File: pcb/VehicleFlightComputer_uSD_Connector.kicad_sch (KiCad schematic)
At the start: 10 parts, among them J5 0472192001

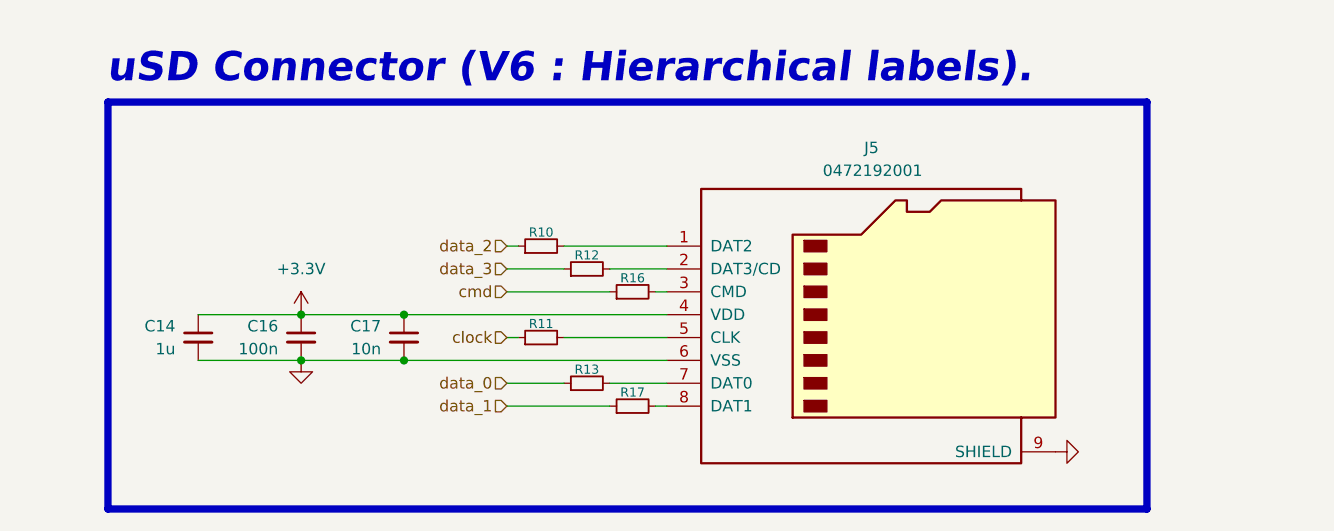
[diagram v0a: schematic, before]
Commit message: Added uSD connector for `VehicleFlightComputer`; added missing solder jumper footprint for LSM6DSV32X.
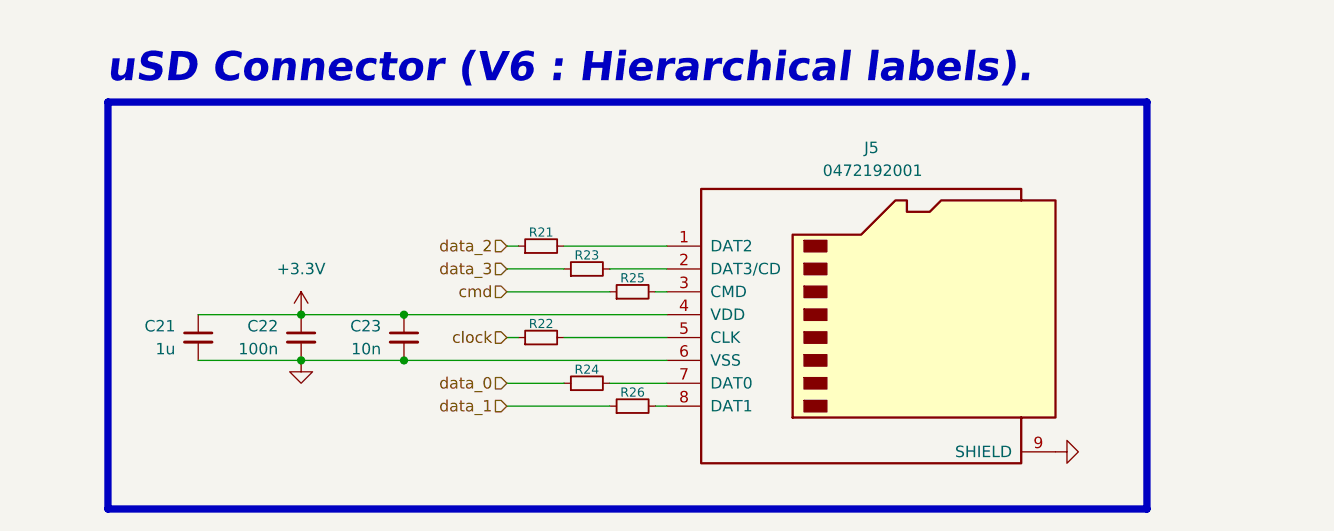
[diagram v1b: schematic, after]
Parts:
- renumbered C14 to C21, C16 to C22, C17 to C23, R10 to R21, R11 to R22, R12 to R23, R13 to R24, R16 to R25, R17 to R26
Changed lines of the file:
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@@
 		(on_board yes)
 		(dnp no)
-		(property "Reference" "R10"
+		(property "Reference" "R21"
 			(at 92.71 68.326 90)
 			(effects
@@
 		(instances
 			(project "VehicleFlightComputer"
-				(path "/378ff2fd-4011-4cd9-8b06-ddd39885e073/6e13037a-c249-4898-9fed-e095c84fcb99"
-					(reference "R10")
+				(path "/378ff2fd-4011-4cd9-8b06-ddd39885e073/759d802d-72f0-4543-9abd-1bdb6f3a2344"
+					(reference "R21")
 					(unit 1)
 				)
@@
 		(on_board yes)
 		(dnp no)
-		(property "Reference" "R11"
+		(property "Reference" "R22"
 			(at 92.71 78.486 90)
 			(effects
@@
 		(instances
 			(project "VehicleFlightComputer"
-				(path "/378ff2fd-4011-4cd9-8b06-ddd39885e073/6e13037a-c249-4898-9fed-e095c84fcb99"
-					(reference "R11")
+				(path "/378ff2fd-4011-4cd9-8b06-ddd39885e073/759d802d-72f0-4543-9abd-1bdb6f3a2344"
+					(reference "R22")
 					(unit 1)
 				)
@@
 		(on_board yes)
 		(dnp no)
-		(property "Reference" "R12"
+		(property "Reference" "R23"
 			(at 97.79 70.866 90)
 			(effects
@@
 		(instances
 			(project "VehicleFlightComputer"
-				(path "/378ff2fd-4011-4cd9-8b06-ddd39885e073/6e13037a-c249-4898-9fed-e095c84fcb99"
-					(reference "R12")
+				(path "/378ff2fd-4011-4cd9-8b06-ddd39885e073/759d802d-72f0-4543-9abd-1bdb6f3a2344"
+					(reference "R23")
 					(unit 1)
 				)
@@
 		(on_board yes)
 		(dnp no)
-		(property "Reference" "R13"
+		(property "Reference" "R24"
 			(at 97.79 83.566 90)
 			(effects
@@
 		(instances
 			(project "VehicleFlightComputer"
-				(path "/378ff2fd-4011-4cd9-8b06-ddd39885e073/6e13037a-c249-4898-9fed-e095c84fcb99"
-					(reference "R13")
+				(path "/378ff2fd-4011-4cd9-8b06-ddd39885e073/759d802d-72f0-4543-9abd-1bdb6f3a2344"
+					(reference "R24")
 					(unit 1)
 				)
@@
 		(on_board yes)
 		(dnp no)
-		(property "Reference" "R16"
+		(property "Reference" "R25"
 			(at 102.87 73.406 90)
 			(effects
@@
 		(instances
 			(project "VehicleFlightComputer"
-				(path "/378ff2fd-4011-4cd9-8b06-ddd39885e073/6e13037a-c249-4898-9fed-e095c84fcb99"
-					(reference "R16")
+				(path "/378ff2fd-4011-4cd9-8b06-ddd39885e073/759d802d-72f0-4543-9abd-1bdb6f3a2344"
+					(reference "R25")
 					(unit 1)
 				)
@@
 		(on_board yes)
 		(dnp no)
-		(property "Reference" "C14"
+		(property "Reference" "C21"
 			(at 52.07 78.7462 0)
 			(effects
@@
 		(instances
 			(project "VehicleFlightComputer"
-				(path "/378ff2fd-4011-4cd9-8b06-ddd39885e073/6e13037a-c249-4898-9fed-e095c84fcb99"
-					(reference "C14")
+				(path "/378ff2fd-4011-4cd9-8b06-ddd39885e073/759d802d-72f0-4543-9abd-1bdb6f3a2344"
+					(reference "C21")
 					(unit 1)
 				)
@@
 		(on_board yes)
 		(dnp no)
-		(property "Reference" "C16"
+		(property "Reference" "C22"
 			(at 63.5 78.7462 0)
 			(effects
@@
 		(instances
 			(project "VehicleFlightComputer"
-				(path "/378ff2fd-4011-4cd9-8b06-ddd39885e073/6e13037a-c249-4898-9fed-e095c84fcb99"
-					(reference "C16")
+				(path "/378ff2fd-4011-4cd9-8b06-ddd39885e073/759d802d-72f0-4543-9abd-1bdb6f3a2344"
+					(reference "C22")
 					(unit 1)
 				)
@@
 		(instances
 			(project "VehicleFlightComputer"
-				(path "/378ff2fd-4011-4cd9-8b06-ddd39885e073/6e13037a-c249-4898-9fed-e095c84fcb99"
+				(path "/378ff2fd-4011-4cd9-8b06-ddd39885e073/759d802d-72f0-4543-9abd-1bdb6f3a2344"
 					(reference "J5")
 					(unit 1)
@@
 		(dnp no)
 		(fields_autoplaced yes)
-		(property "Reference" "#PWR033"
+		(property "Reference" "#PWR076"
 			(at 66.04 88.9 0)
 			(effects
@@
 		(instances
 			(project "VehicleFlightComputer"
-				(path "/378ff2fd-4011-4cd9-8b06-ddd39885e073/6e13037a-c249-4898-9fed-e095c84fcb99"
-					(reference "#PWR033")
+				(path "/378ff2fd-4011-4cd9-8b06-ddd39885e073/759d802d-72f0-4543-9abd-1bdb6f3a2344"
+					(reference "#PWR076")
 					(unit 1)
 				)
@@
 		(dnp no)
 		(fields_autoplaced yes)
-		(property "Reference" "#PWR032"
+		(property "Reference" "#PWR075"
 			(at 66.04 81.28 0)
 			(effects
@@
 		(instances
 			(project "VehicleFlightComputer"
-				(path "/378ff2fd-4011-4cd9-8b06-ddd39885e073/6e13037a-c249-4898-9fed-e095c84fcb99"
-					(reference "#PWR032")
+				(path "/378ff2fd-4011-4cd9-8b06-ddd39885e073/759d802d-72f0-4543-9abd-1bdb6f3a2344"
+					(reference "#PWR075")
 					(unit 1)
 				)
@@
 		(dnp no)
 		(fields_autoplaced yes)
-		(property "Reference" "#PWR037"
+		(property "Reference" "#PWR077"
 			(at 156.21 92.71 0)
 			(effects
@@
 		(instances
 			(project "VehicleFlightComputer"
-				(path "/378ff2fd-4011-4cd9-8b06-ddd39885e073/6e13037a-c249-4898-9fed-e095c84fcb99"
-					(reference "#PWR037")
+				(path "/378ff2fd-4011-4cd9-8b06-ddd39885e073/759d802d-72f0-4543-9abd-1bdb6f3a2344"
+					(reference "#PWR077")
 					(unit 1)
 				)
@@
 		(on_board yes)
 		(dnp no)
-		(property "Reference" "R17"
+		(property "Reference" "R26"
 			(at 102.87 86.106 90)
 			(effects
@@
 		(instances
 			(project "VehicleFlightComputer"
-				(path "/378ff2fd-4011-4cd9-8b06-ddd39885e073/6e13037a-c249-4898-9fed-e095c84fcb99"
-					(reference "R17")
+				(path "/378ff2fd-4011-4cd9-8b06-ddd39885e073/759d802d-72f0-4543-9abd-1bdb6f3a2344"
+					(reference "R26")
 					(unit 1)
 				)
@@
 		(on_board yes)
 		(dnp no)
-		(property "Reference" "C17"
+		(property "Reference" "C23"
 			(at 74.93 78.7462 0)
 			(effects
@@
 		(instances
 			(project "VehicleFlightComputer"
-				(path "/378ff2fd-4011-4cd9-8b06-ddd39885e073/6e13037a-c249-4898-9fed-e095c84fcb99"
-					(reference "C17")
-					(unit 1)
-				)
+				(path "/378ff2fd-4011-4cd9-8b06-ddd39885e073/759d802d-72f0-4543-9abd-1bdb6f3a2344"
+					(reference "C23")
+					(unit 1)
+				)

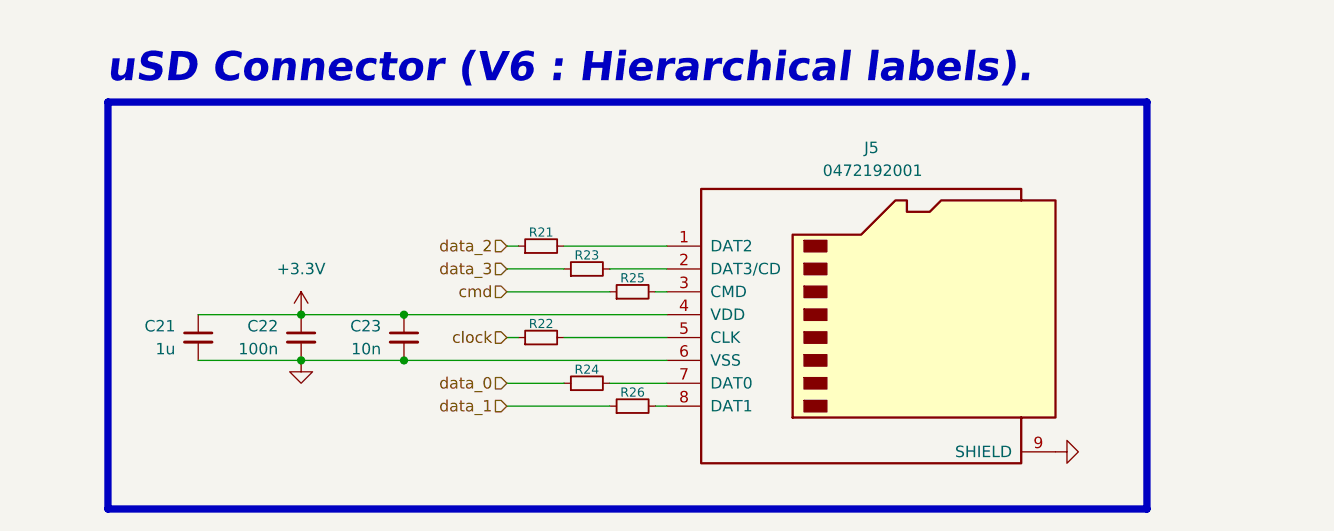
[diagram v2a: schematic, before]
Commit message: Addressed ERC schematic issues for `VehicleFlightComputer`.
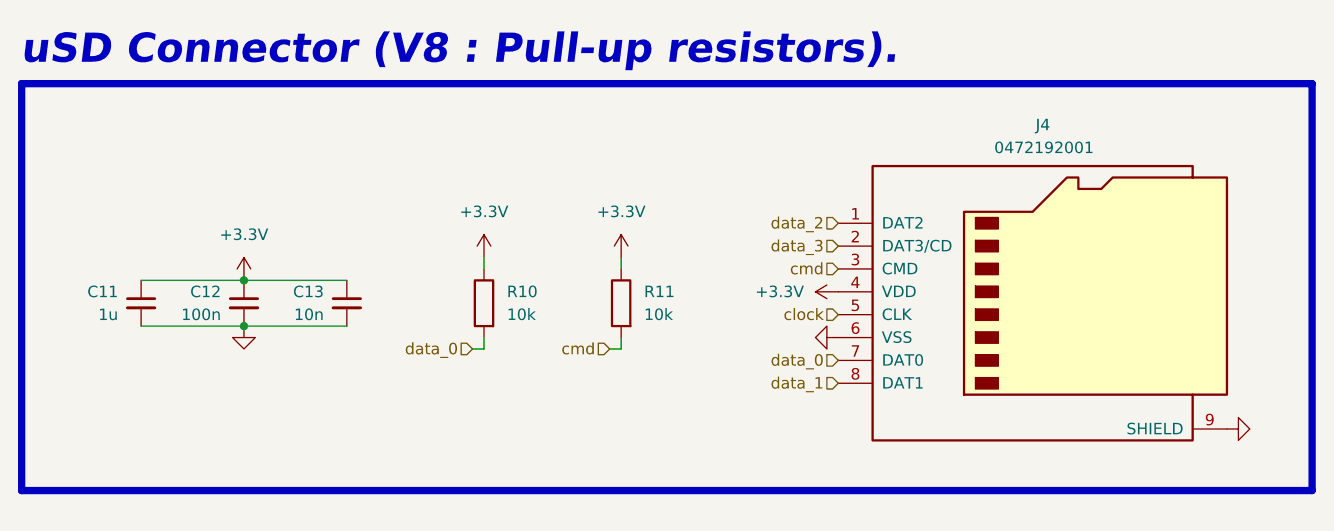
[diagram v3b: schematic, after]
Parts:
- removed R21, R22, R23, R24, R25, R26: R_Small, Resistor_SMD:R_1206_3216Metric_Pad1.30x1.75mm_HandSolder, symbol Device:R_Small
- added R10, R11: 10k, Resistor_SMD:R_1206_3216Metric_Pad1.30x1.75mm_HandSolder, symbol Device:R
- renumbered C21 to C11, C22 to C12, C23 to C13, J5 to J4
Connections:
- net +3.3V: now also R10.1, R11.1
- net clock: now also J4.5 (CLK)
- net cmd: now also J4.3 (CMD), R11.2
- net data_0: now also J4.7 (DAT0), R10.2
- net data_1: now also J4.8 (DAT1)
- net data_2: now also J4.1 (DAT2)
- net data_3: now also J4.2 (DAT3/CD)
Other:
- note added: "uSD Connector (V8 : Pull-up resistors)."
- note removed: "uSD Connector (V6 : Hierarchical labels)."
- moved on the sheet: C11, C12, C13, J4

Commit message: Revised `VehicleFlightComputer`.
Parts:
- renumbered C13 to C12, C11 to C13, C12 to C2, R11 to R3, R10 to R4
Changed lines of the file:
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@@
 		(on_board yes)
 		(dnp no)
-		(property "Reference" "R11"
+		(property "Reference" "R3"
 			(at 104.14 74.9299 0)
 			(effects
@@
 			)
 		)
-		(property "Datasheet" "~"
+		(property "Datasheet" ""
 			(at 101.6 76.2 0)
 			(effects
@@
 			)
 		)
-		(property "Description" "Resistor"
+		(property "Description" ""
 			(at 101.6 76.2 0)
 			(effects
@@
 			(project ""
 				(path "/378ff2fd-4011-4cd9-8b06-ddd39885e073/759d802d-72f0-4543-9abd-1bdb6f3a2344"
-					(reference "R11")
+					(reference "R3")
 					(unit 1)
 				)
@@
 		(on_board yes)
 		(dnp no)
-		(property "Reference" "C11"
+		(property "Reference" "C13"
 			(at 45.72 74.9362 0)
 			(effects
@@
 			)
 		)
-		(property "Datasheet" "~"
+		(property "Datasheet" ""
 			(at 48.26 76.2 0)
 			(effects
@@
 			)
 		)
-		(property "Description" "Unpolarized capacitor, small symbol"
+		(property "Description" ""
 			(at 48.26 76.2 0)
 			(effects
@@
 			(project ""
 				(path "/378ff2fd-4011-4cd9-8b06-ddd39885e073/759d802d-72f0-4543-9abd-1bdb6f3a2344"
-					(reference "C11")
+					(reference "C13")
 					(unit 1)
 				)
@@
 		(on_board yes)
 		(dnp no)
-		(property "Reference" "C12"
+		(property "Reference" "C2"
 			(at 57.15 74.9362 0)
 			(effects
@@
 			)
 		)
-		(property "Datasheet" "~"
+		(property "Datasheet" ""
 			(at 59.69 76.2 0)
 			(effects
@@
 			)
 		)
-		(property "Description" "Unpolarized capacitor, small symbol"
+		(property "Description" ""
 			(at 59.69 76.2 0)
 			(effects
@@
 			(project ""
 				(path "/378ff2fd-4011-4cd9-8b06-ddd39885e073/759d802d-72f0-4543-9abd-1bdb6f3a2344"
-					(reference "C12")
+					(reference "C2")
 					(unit 1)
 				)
@@
 			)
 		)
-		(property "Datasheet" "https://www.we-online.com/components/products/datasheet/693072010801.pdf"
+		(property "Datasheet" ""
 			(at 148.59 74.93 0)
 			(effects
@@
 			)
 		)
-		(property "Description" "Micro SD Card Socket"
+		(property "Description" ""
 			(at 148.59 74.93 0)
 			(effects
@@
 		(on_board yes)
 		(dnp no)
-		(property "Reference" "R10"
+		(property "Reference" "R4"
 			(at 88.9 74.9299 0)
 			(effects
@@
 			)
 		)
-		(property "Datasheet" "~"
+		(property "Datasheet" ""
 			(at 86.36 76.2 0)
 			(effects
@@
 			)
 		)
-		(property "Description" "Resistor"
+		(property "Description" ""
 			(at 86.36 76.2 0)
 			(effects
@@
 			(project ""
 				(path "/378ff2fd-4011-4cd9-8b06-ddd39885e073/759d802d-72f0-4543-9abd-1bdb6f3a2344"
-					(reference "R10")
+					(reference "R4")
 					(unit 1)
 				)
@@
 		(on_board yes)
 		(dnp no)
-		(property "Reference" "C13"
+		(property "Reference" "C12"
 			(at 68.58 74.9362 0)
 			(effects
@@
 			)
 		)
-		(property "Datasheet" "~"
+		(property "Datasheet" ""
 			(at 71.12 76.2 0)
 			(effects
@@
 			)
 		)
-		(property "Description" "Unpolarized capacitor, small symbol"
+		(property "Description" ""
 			(at 71.12 76.2 0)
 			(effects
@@
 			(project ""
 				(path "/378ff2fd-4011-4cd9-8b06-ddd39885e073/759d802d-72f0-4543-9abd-1bdb6f3a2344"
-					(reference "C13")
-					(unit 1)
-				)
+					(reference "C12")
+					(unit 1)
+				)

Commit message: Finalized `VFC-R2`.
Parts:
- renumbered R4 to R3, R3 to R4
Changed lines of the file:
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@@
 		(on_board yes)
 		(dnp no)
-		(property "Reference" "R3"
+		(property "Reference" "R4"
 			(at 104.14 74.9299 0)
 			(effects
@@
 			(project ""
 				(path "/378ff2fd-4011-4cd9-8b06-ddd39885e073/759d802d-72f0-4543-9abd-1bdb6f3a2344"
-					(reference "R3")
+					(reference "R4")
 					(unit 1)
 				)
@@
 		(on_board yes)
 		(dnp no)
-		(property "Reference" "R4"
+		(property "Reference" "R3"
 			(at 88.9 74.9299 0)
 			(effects
@@
 			(project ""
 				(path "/378ff2fd-4011-4cd9-8b06-ddd39885e073/759d802d-72f0-4543-9abd-1bdb6f3a2344"
-					(reference "R4")
-					(unit 1)
-				)
+					(reference "R3")
+					(unit 1)
+				)
